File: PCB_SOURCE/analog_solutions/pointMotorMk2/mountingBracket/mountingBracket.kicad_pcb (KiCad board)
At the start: 2 copper layers, 20 x 24.2 mm, 16 parts

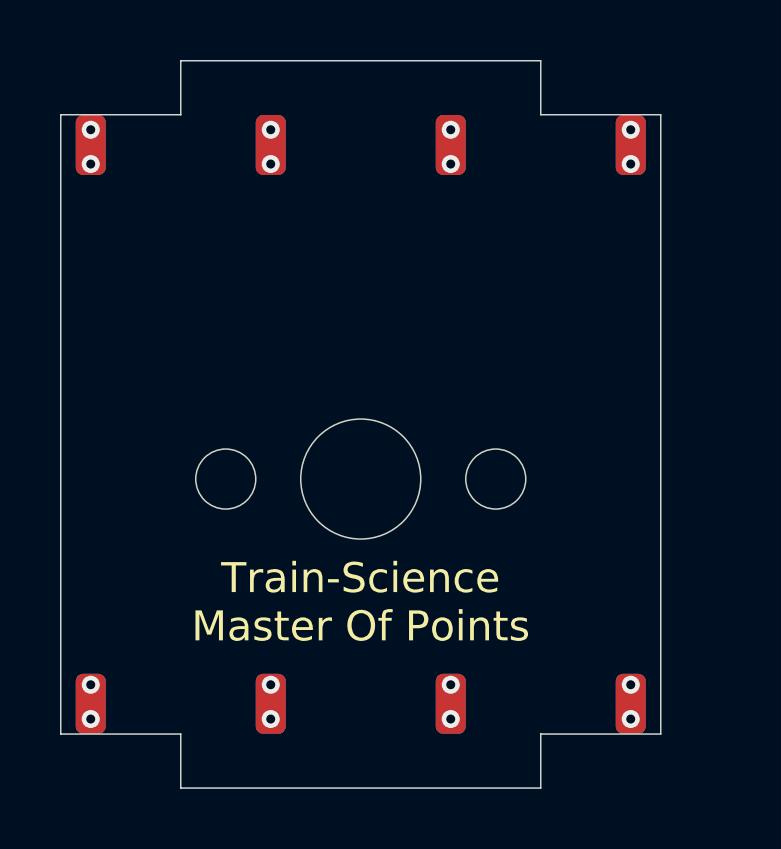
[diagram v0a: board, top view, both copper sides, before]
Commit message: fixed bug in ahob program among others
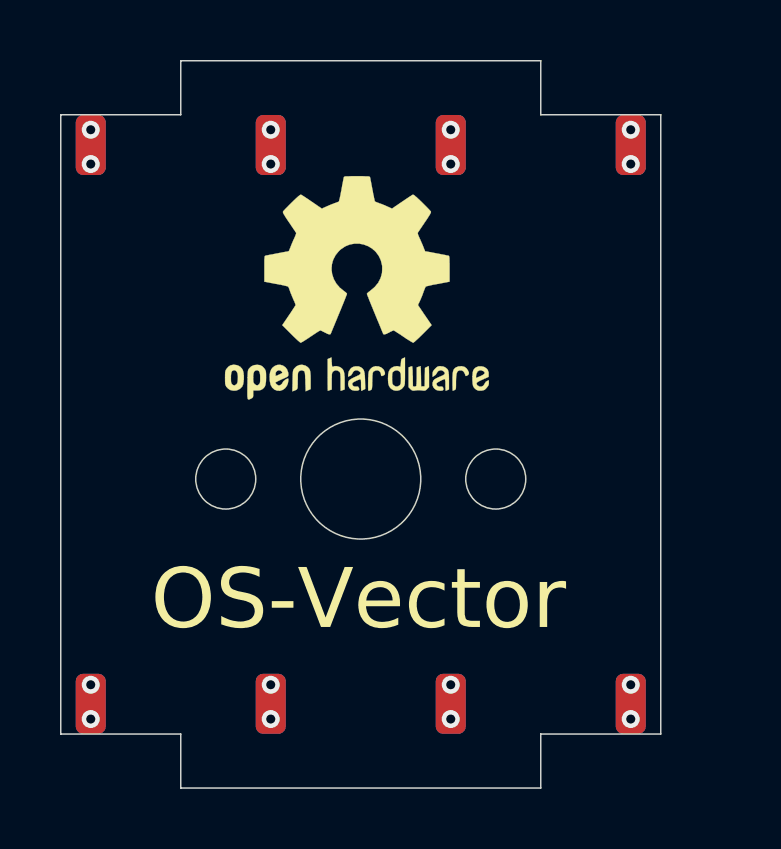
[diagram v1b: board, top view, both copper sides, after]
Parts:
- added REF**: OSHW-Logo2_9.8x8mm_SilkScreen, Symbol:OSHW-Logo2_9.8x8mm_SilkScreen, F.Cu at (-0.13, -0.38)
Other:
- board text added: "OS-Vector"
- board text removed: "Train-Science Master Of Points"
